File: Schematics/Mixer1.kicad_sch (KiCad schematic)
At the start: 56 parts

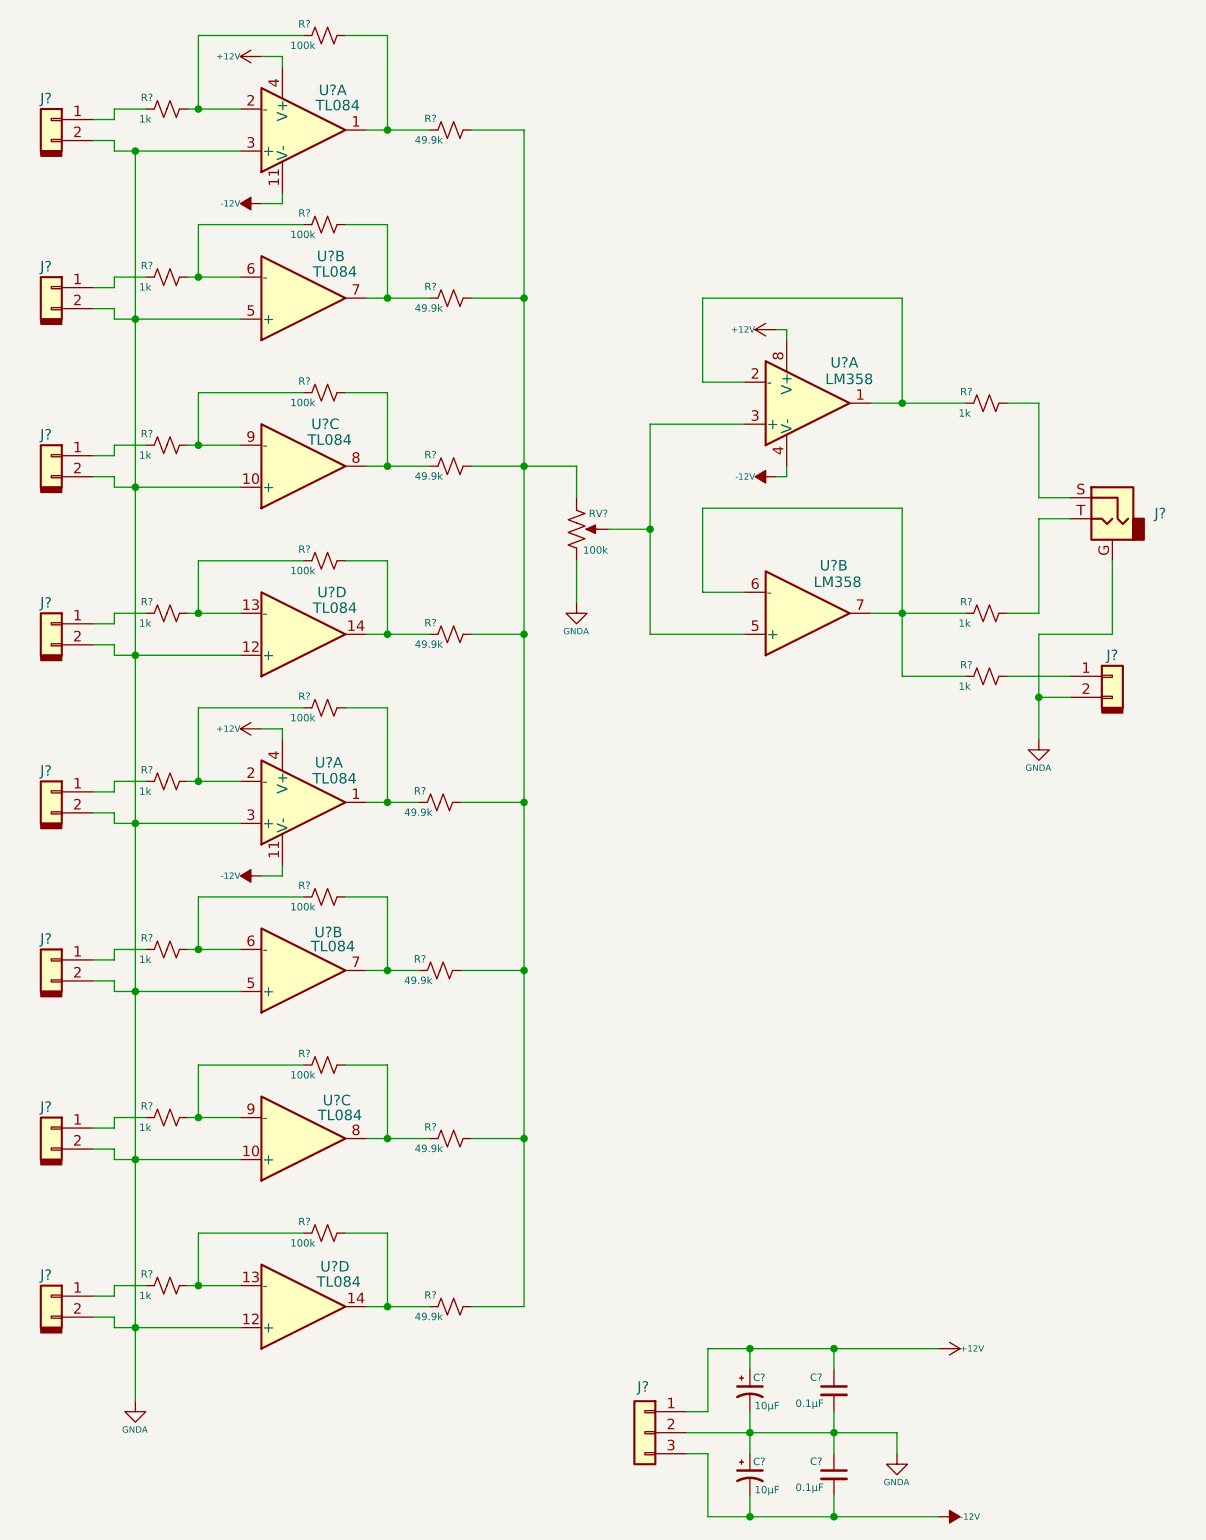
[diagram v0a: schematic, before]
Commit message: - Updated current libraries - New 7 inc display with ESP32S3 and second USB upload port - Start of I2C feeder interface slave on display.
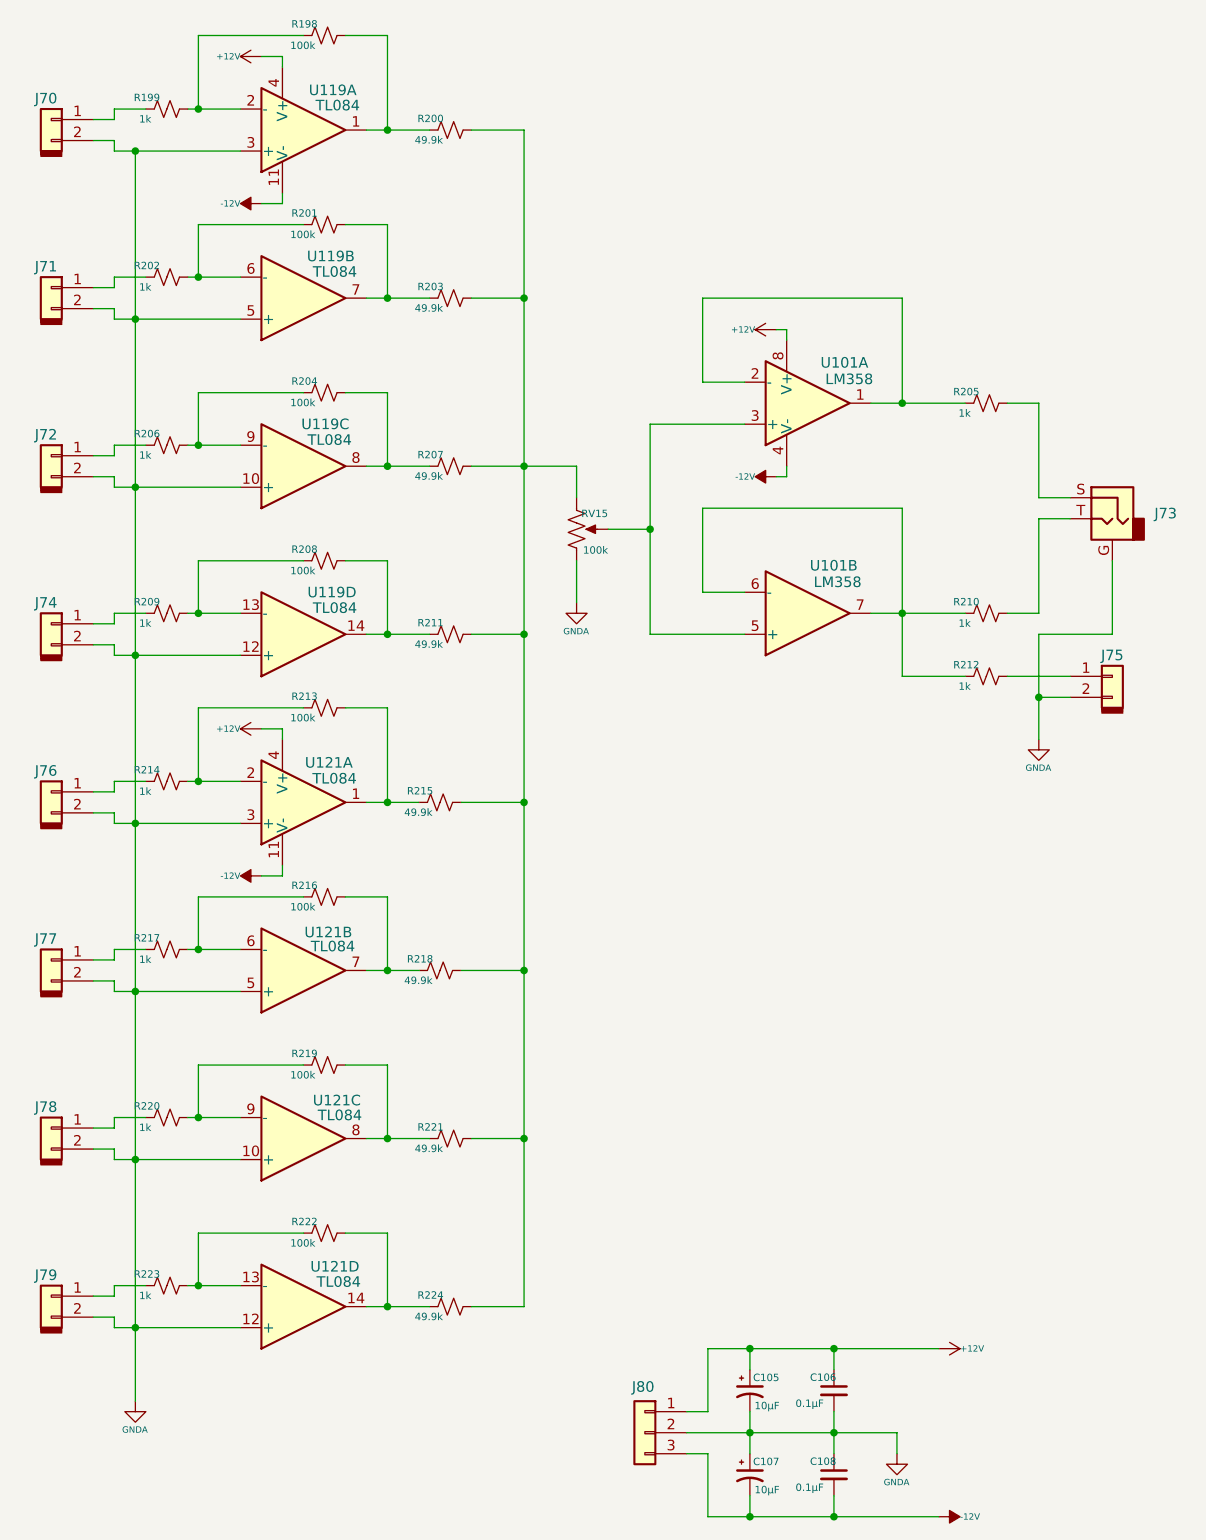
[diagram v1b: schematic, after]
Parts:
- gave numbers to parts that had none: 47

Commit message: updated schematics.
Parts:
- removed J74, J76, J77, J78, J79: Conn_01x02, symbol Connector_keyed_kicad_sym:Conn_01x02
- removed R198, R201, R204, R208, R213, R216, R219, R222: 100k, symbol Device:R_Small_US
- removed R199, R202, R205, R206, R209, R212, R214, R217, R220, R223: 1k, symbol Device:R_Small_US
- removed R200, R203, R207, R211, R215, R218, R221, R224: 49.9k, symbol Device:R_Small_US
- removed U101, U120: LM358, symbol Amplifier_Operational:LM358
- removed U119, U121: TL084, symbol Amplifier_Operational:TL084
- added C105, C106, C107, C108, C129, C130, C131, C132, C49, C50: 10µF, symbol Device:C_Small
- added C135, C136: 0.1µF, symbol Device:C_Small
- added J57, J58, J61, J63, J64, J65, J72: Conn_01x02, symbol Connector_keyed_kicad_sym:Conn_01x02
- added R125, R126, R127, R128, R129, R130, R73, R74, R78, R79: 47k, symbol Device:R_Small_US
- added R131, R133: 20k, symbol Device:R_Small_US
- added R132: 10k, symbol Device:R_Small_US
- added R135, R136: 1k, symbol Device:R_Small_US
- added RV8: 100k, symbol Device:R_Potentiometer_US
- added U16: LME49720N, symbol Amplifier_Operational:TL072
- renumbered C106 to C133, C108 to C134, C105 to C47, C107 to C48, J72 to J62, J80 to J73, J73 to J74, R210 to R134, RV15 to RV9
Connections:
- net +12V: now also C135.1, U16.8 (V+)
- net -12V: now also C136.2, U16.4 (V-)
- net GNDA: now also C135.2, C136.1, J57.2 (Pin_2), J58.2 (Pin_2), J61.2 (Pin_2), J63.2 (Pin_2), J64.2 (Pin_2), J65.2 (Pin_2), J72.2 (Pin_2), U16.3 (+), U16.5 (+)
- net at R134.1: now also R133.2, R135.1, U16.7
- net at J75.1 (Pin_1): now also R136.2
- net at J62.1 (Pin_1): now also C106.1
- net at J74.S: now also R135.2
- net at J70.1 (Pin_1): now also C130.1
- net at J71.1 (Pin_1): now also C131.1
- new net: C49.2, R73.1
- new net: R125.2, R126.2, R127.2, R128.2, R129.2, R130.2, R131.1, R73.2, R74.2, R78.2, R79.2, U16.2 (-)
- new net: C130.2, R128.1
- new net: C106.2, R79.1
- new net: C107.1, J63.1 (Pin_1)
- new net: C107.2, R125.1
- new net: C49.1, J57.1 (Pin_1)
- new net: C132.2, R130.1
- new net: C132.1, J72.1 (Pin_1)
- new net: R136.1, RV8. (3), RV9. (3), U16.1
- new net: R132.1, RV9. (3)
- new net: R132.2, R133.1, U16.6 (-)
- new net: C129.1, J65.1 (Pin_1)
- new net: C129.2, R127.1
- new net: C105.2, R78.1
- new net: R131.2, RV8. (3)
- new net: C50.2, R74.1
- new net: C105.1, J61.1 (Pin_1)
- new net: C50.1, J58.1 (Pin_1)
- new net: C108.2, R126.1
- new net: C131.2, R129.1
- new net: C108.1, J64.1 (Pin_1)
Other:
- moved on the sheet: C133, C134, C47, C48, J62, J73, J74, J75, R134, RV9

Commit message: Upgreade byte value interface to short.  First stage of refactoring midi input for rotory encoders.  Still needs scaling.
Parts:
- renumbered C47 to C37, C48 to C38, C49 to C39, C50 to C40, C105 to C41, C106 to C42, C107 to C43, C108 to C44, C129 to C45, C130 to C46, C131 to C47, C132 to C48, C133 to C49, C134 to C50, C135 to C51, C136 to C52, J57 to J20, J58 to J21, J61 to J22, J62 to J23, J63 to J24, J64 to J25, J65 to J26, J70 to J27, J71 to J28, J72 to J29, J73 to J30, J75 to J31, J74 to J32, R73 to R119, R74 to R120, R78 to R121, R79 to R122, R125 to R123, R126 to R124, R127 to R125, R128 to R126, R129 to R127, R130 to R128, R131 to R129, R132 to R130, R133 to R131, R134 to R132, R136 to R133, R135 to R134, RV8 to RV6, RV9 to RV7, U16 to U46

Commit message: Updated schematics including VCO and VCF daughter boards
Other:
- company:       MLE Tech                  Cedar Park, TX -> (none)
- title: Synth #2 -> Ten Channel Mixer
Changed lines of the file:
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@@
 	(paper "USLegal")
 	(title_block
-		(title "Synth #2")
-		(date "2023-07-27")
-		(rev "0.1")
-		(company "      MLE Tech                  Cedar Park, TX")
-		(comment 2 "In Development")
+		(title "Ten Channel Mixer")
+		(date "2025-01-16")
+		(rev "2.0")
+		(comment 1 "In Development ")
 	)
 	(junction

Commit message: Final tweaks on LFO interfaces and tuning.  Update display layouts.
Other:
- note added: "Audio Out"
- note added: "Monitor Accessories"
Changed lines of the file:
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@@
+		)
+	)
+	(text "Monitor\nAccessories"
+		(exclude_from_sim no)
+		(at 158.1589 69.0164 0)
+		(effects
+			(font
+				(size 1.27 1.27)
+			)
+		)
+	)
+	(text "Audio\nOut"
+		(exclude_from_sim no)
+		(at 157.5778 82.6141 0)
+		(effects
+			(font
+				(size 1.27 1.27)
+			)
 		)
 	)
@@
 		(on_board yes)
 		(dnp no)
-		(fields_autoplaced yes)
 		(property "Reference" "J32"
-			(at 154.94 81.9149 0)
-			(effects
-				(font
+			(at 148.082 77.47 0)
+			(effects
+				(font

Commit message: Cleaned up page advance on display controls.
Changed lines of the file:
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@@
 (kicad_sch
-	(version 20231120)
+	(version 20250114)
 	(generator "eeschema")
-	(generator_version "8.0")
+	(generator_version "9.0")
 	(paper "USLegal")
 	(title_block
@@
 		(comment 1 "In Development ")
 	)
+	(text "Monitor\nAccessories"
+		(exclude_from_sim no)
+		(at 158.1589 69.0164 0)
+		(effects
+			(font
+				(size 1.27 1.27)
+			)
+		)
+	)
+	(text "Audio\nOut"
+		(exclude_from_sim no)
+		(at 157.5778 82.6141 0)
+		(effects
+			(font
+				(size 1.27 1.27)
+			)
+		)
+	)
 	(junction
 		(at 36.83 33.02)
@@
 		)
 	)
-	(text "Monitor\nAccessories"
-		(exclude_from_sim no)
-		(at 158.1589 69.0164 0)
-		(effects
-			(font
-				(size 1.27 1.27)
-			)
-		)
-	)
-	(text "Audio\nOut"
-		(exclude_from_sim no)
-		(at 157.5778 82.6141 0)
-		(effects
-			(font
-				(size 1.27 1.27)
-			)
-		)
-	)
 	(symbol
 		(lib_id "Device:R_Small_US")
@@
 		)
 	)
+	(embedded_fonts no)
 )

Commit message: Fixed bugs in voice selection on configuration.  Reorganized schematics to have different master drawings for power and audio paths.  Started work on dual 3-pole state variable filter with resonance.
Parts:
- renumbered C38 to C174, C39 to C175, C40 to C176, C41 to C177, C42 to C178, C43 to C179, C44 to C180, C45 to C183, C46 to C184, C47 to C185, C48 to C186, C49 to C187, C50 to C188, C51 to C189, C52 to C190, C37 to C69, J20 to J111, J21 to J112, J22 to J113, J23 to J117, J24 to J118, J25 to J119, J26 to J120, J27 to J121, J28 to J122, J29 to J123, J30 to J124, J31 to J125, J32 to J126, R119 to R180, R120 to R265, R121 to R267, R122 to R268, R123 to R269, R124 to R270, R125 to R271, R126 to R272, R127 to R273, R128 to R318, R129 to R319, R130 to R328, R131 to R329, R132 to R330, R133 to R331, R134 to R332, RV6 to RV17, RV7 to RV18, U46 to U108

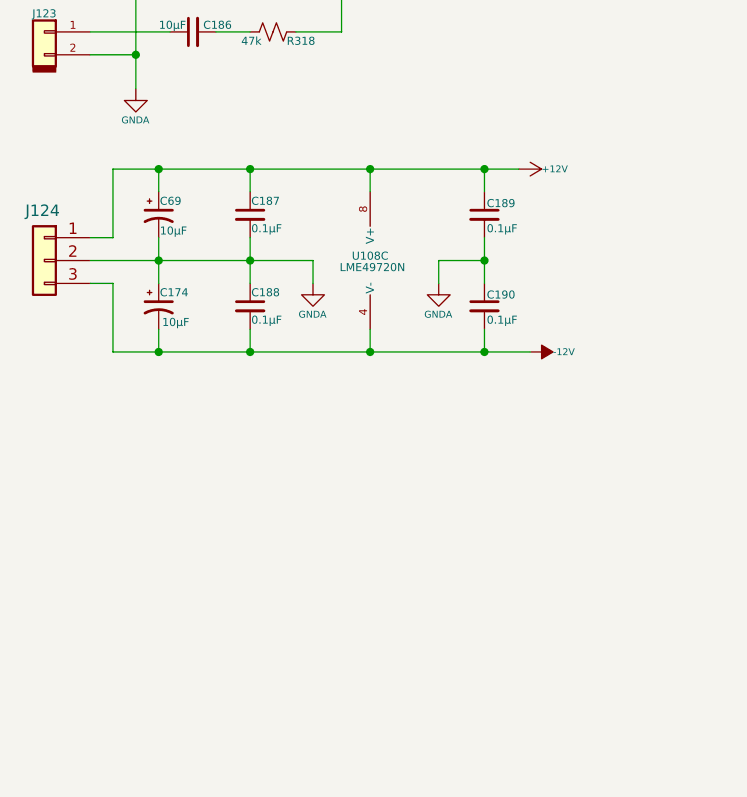
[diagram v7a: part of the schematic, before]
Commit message: Fixed schematic errors.
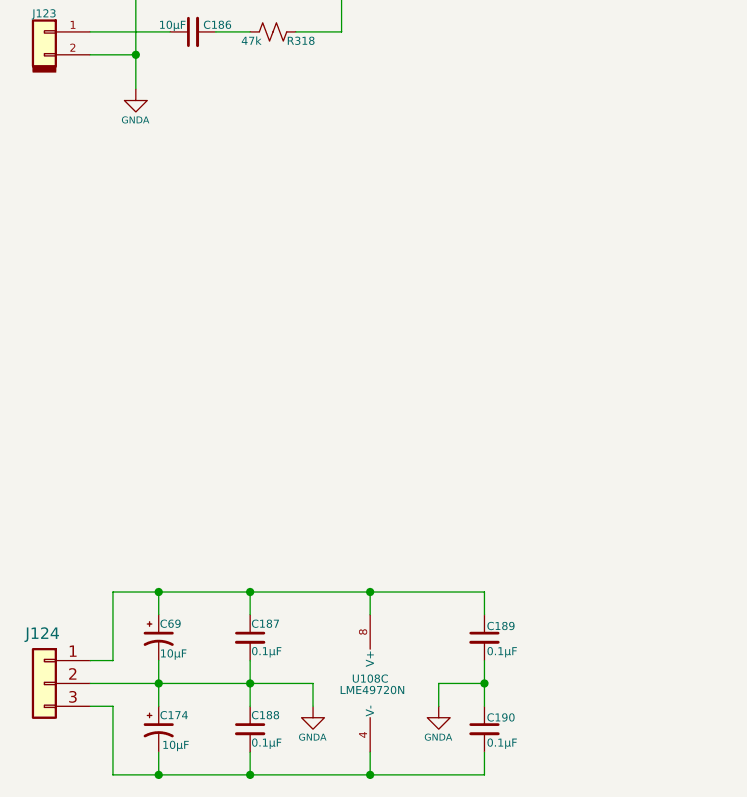
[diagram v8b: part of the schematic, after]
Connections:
- net +12V: no longer names the net of C187.1, C189.1, C69.1, J124.1 (Pin_1), U108.8 (V+)
- net -12V: no longer names the net of C174.2, C188.2, C190.2, J124.3 (Pin_3), U108.4 (V-)
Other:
- moved on the sheet: C174, C187, C188, C189, C190, C69, J124, U108C
